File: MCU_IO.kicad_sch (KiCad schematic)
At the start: 27 parts, among them J1 Conn_02x07_Odd_Even, J10 Conn_01x05, U7 TMS320F28379DPTPQ, U8 M24512, U9 MAX809, Y1 10 MHz

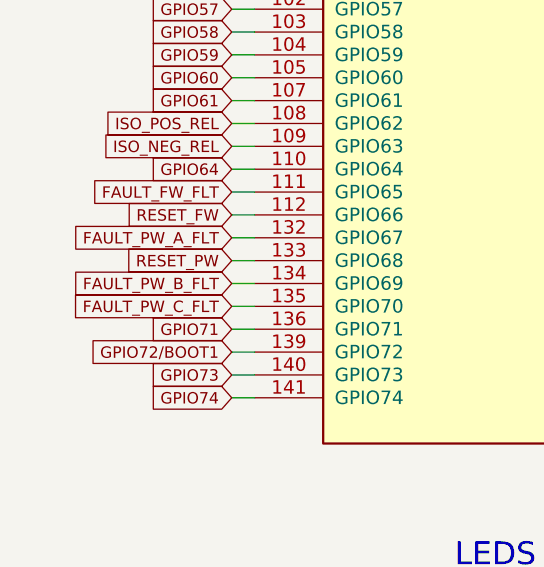
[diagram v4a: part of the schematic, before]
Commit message: Изменения: добавил 3или для фолтов трёхфазного модуля
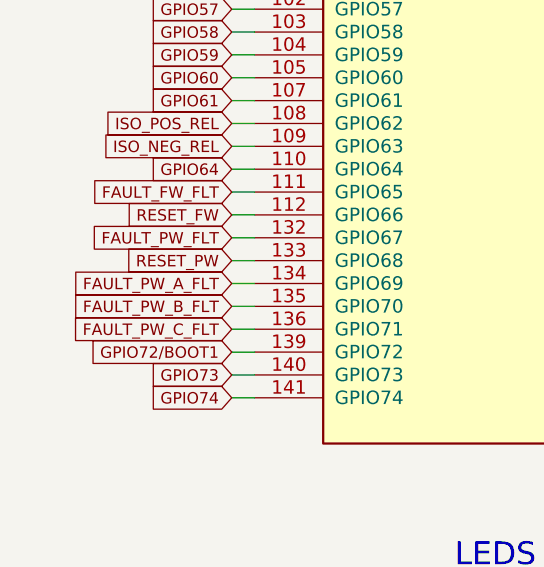
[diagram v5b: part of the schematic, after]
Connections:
- net GPIO71 is gone; now on net FAULT_PW_C_FLT: U7.136 (GPIO71)
- net FAULT_PW_A_FLT: now also U7.134 (GPIO69); no longer U7.132 (GPIO67)
- net FAULT_PW_B_FLT: now also U7.135 (GPIO70); no longer U7.134 (GPIO69)
- net FAULT_PW_C_FLT: no longer U7.135 (GPIO70)
- new net FAULT_PW_FLT: U7.132 (GPIO67)
